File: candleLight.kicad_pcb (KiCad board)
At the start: 2 copper layers, 59 x 29.6 mm, 44 parts, among them J1 USB_C_Receptacle_USB2.0, J2 Conn_Phoenix, J3 Conn_SWD, J4 Conn_IO, J5 Conn_BOOT0, J6 Conn_CAN_Jumper, J7 Conn_5V, U1 STM32F072C8Tx, U2 AMS1117-3.3, U3 TJA1051TK-3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

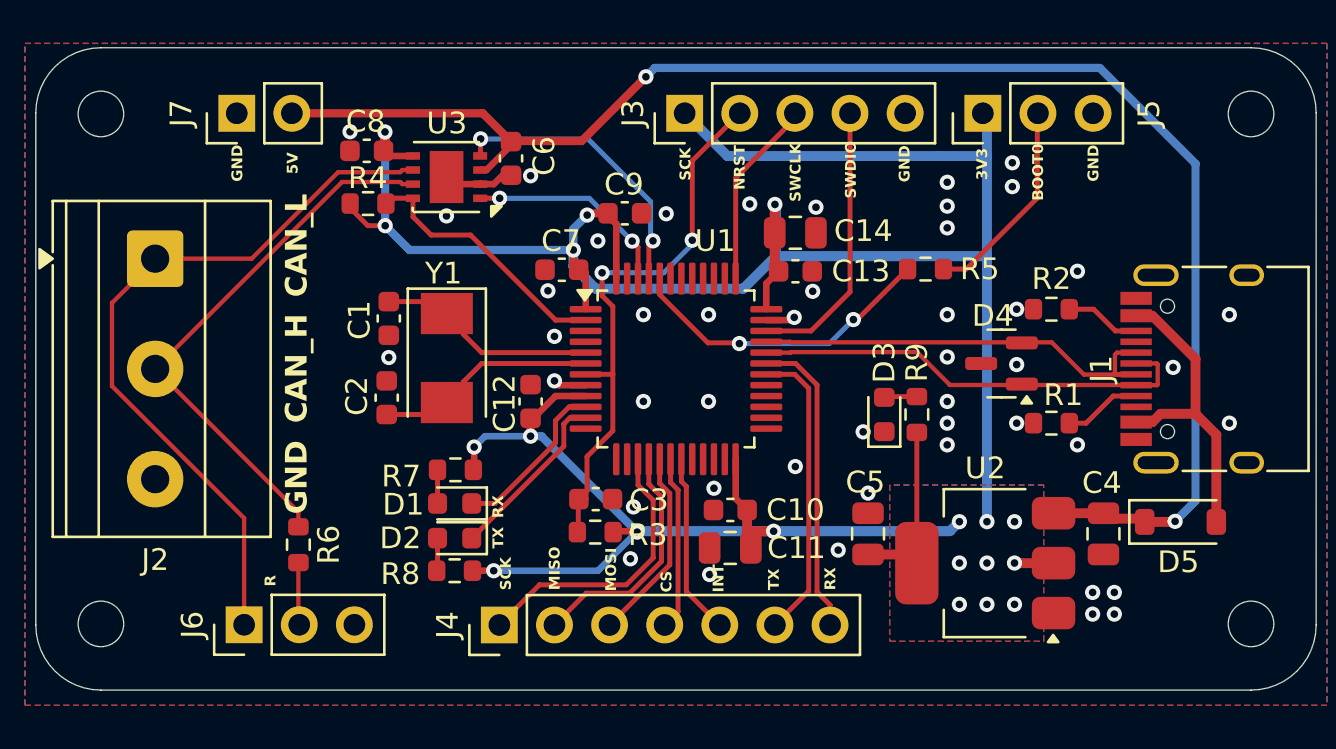
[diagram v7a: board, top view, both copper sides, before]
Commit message: update load caps
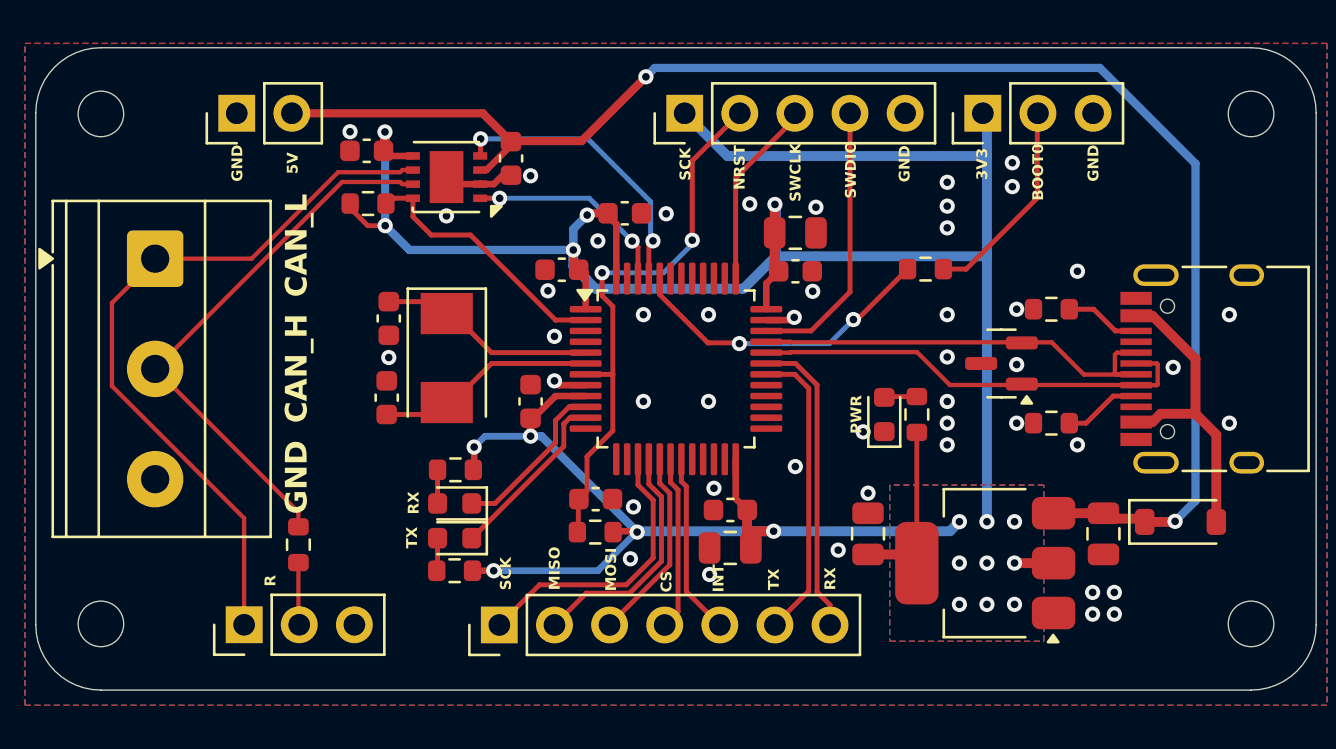
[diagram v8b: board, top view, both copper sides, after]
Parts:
- C1, C2: value 20pF -> 30pF
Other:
- board text added: "PWR"
- board text added: "candleLight v2.1"
- board text removed: "candleLight V2.1"
